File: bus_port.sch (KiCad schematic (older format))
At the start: 3 parts

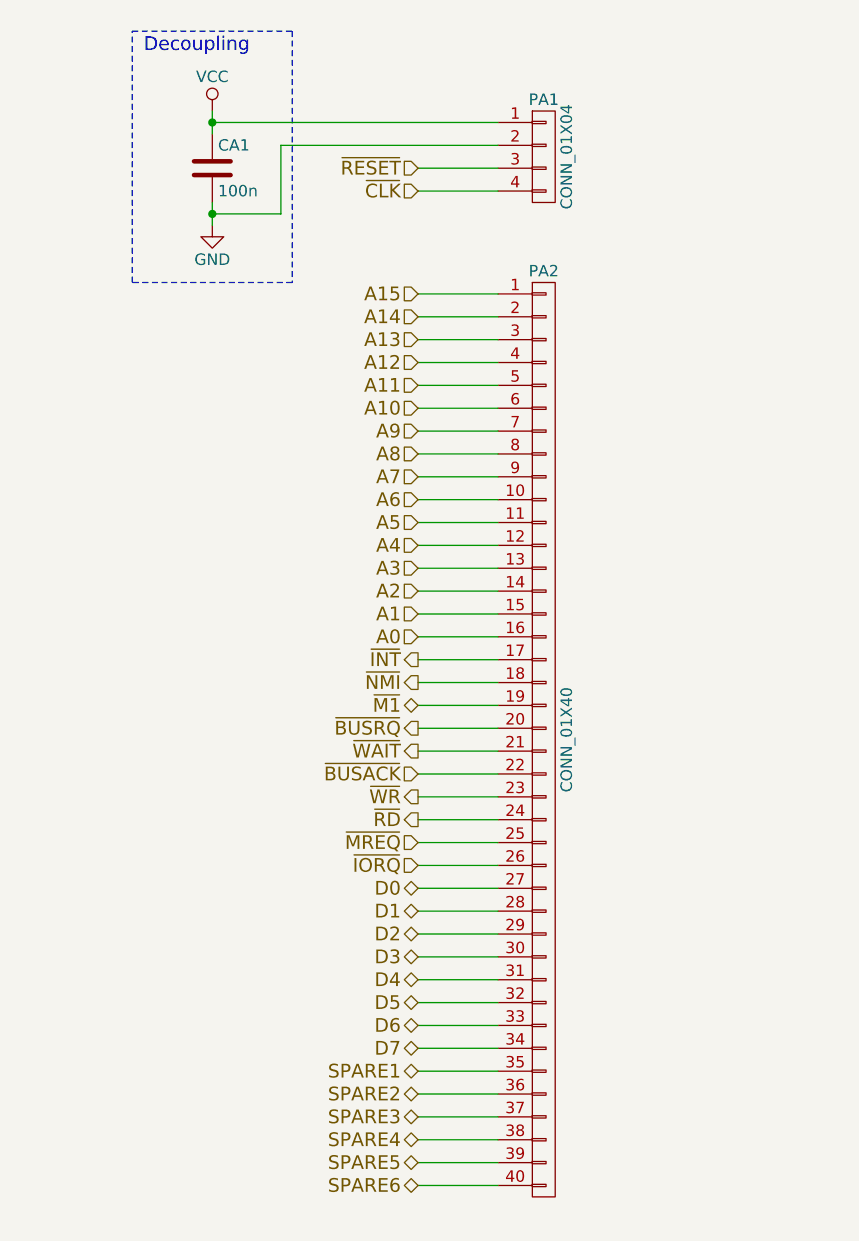
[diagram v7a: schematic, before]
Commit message: New layout complete. Now with rc2014 compat. slots!
Plus on board address decoding, single stepping using M1 line so button
is click per instruction. Board is also much smaller!
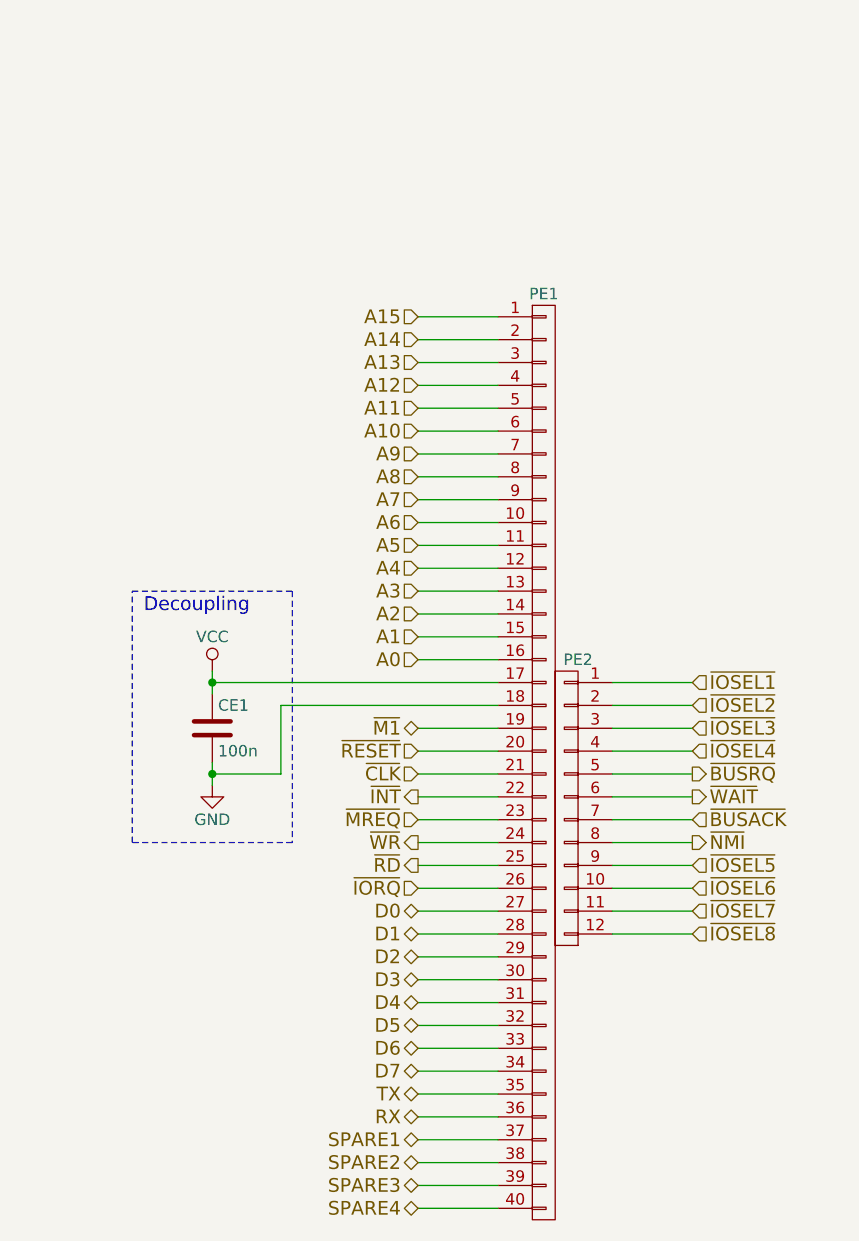
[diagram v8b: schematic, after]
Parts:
- removed PA1: CONN_01X04, Socket_Strips:Socket_Strip_Straight_1x04, symbol CONN_01X04
- removed PA2: CONN_01X40, Socket_Strips:Socket_Strip_Straight_1x40, symbol CONN_01X40
- added PA1: CONN_01X40, Socket_Strips:Socket_Strip_Straight_1x40, symbol CONN_01X40
- added PA2: CONN_01X12, Socket_Strips:Socket_Strip_Straight_1x12, symbol CONN_01X12
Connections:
- net A0: now also PA1.16 (P16)
- net A1: now also PA1.15 (P15)
- net A10: now also PA1.6 (P6)
- net A11: now also PA1.5 (P5)
- net A12: now also PA1.4 (P4)
- net A13: now also PA1.3 (P3)
- net A14: now also PA1.2 (P2)
- net A15: now also PA1.1 (P1)
- net A2: now also PA1.14 (P14)
- net A3: now also PA1.13 (P13)
- net A4: now also PA1.12 (P12)
- net A5: now also PA1.11 (P11)
- net A6: now also PA1.10 (P10)
- net A7: now also PA1.9 (P9)
- net A8: now also PA1.8 (P8)
- net A9: now also PA1.7 (P7)
- net D0: now also PA1.27 (P27)
- net D1: now also PA1.28 (P28)
- net D2: now also PA1.29 (P29)
- net D3: now also PA1.30 (P30)
- net D4: now also PA1.31 (P31)
- net D5: now also PA1.32 (P32)
- net D6: now also PA1.33 (P33)
- net D7: now also PA1.34 (P34)
- net GND: now also PA1.18 (P18)
- net SPARE1: now also PA1.37 (P37)
- net SPARE2: now also PA1.38 (P38)
- net SPARE3: now also PA1.39 (P39)
- net SPARE4: now also PA1.40 (P40)
- net VCC: now also PA1.17 (P17)
- net ~BUSACK: now also PA2.7 (P7)
- net ~BUSRQ: now also PA2.5 (P5)
- net ~CLK: now also PA1.21 (P21)
- net ~INT: now also PA1.22 (P22)
- net ~IORQ: now also PA1.26 (P26)
- net ~M1: now also PA1.19 (P19)
- net ~MREQ: now also PA1.23 (P23)
- net ~NMI: now also PA2.8 (P8)
- net ~RD: now also PA1.25 (P25)
- net ~RESET: now also PA1.20 (P20)
- net ~WAIT: now also PA2.6 (P6)
- net ~WR: now also PA1.24 (P24)
- new net RX: PA1.36 (P36)
- new net TX: PA1.35 (P35)
- new net ~IOSEL1: PA2.1 (P1)
- new net ~IOSEL2: PA2.2 (P2)
- new net ~IOSEL3: PA2.3 (P3)
- new net ~IOSEL4: PA2.4 (P4)
- new net ~IOSEL5: PA2.9 (P9)
- new net ~IOSEL6: PA2.10 (P10)
- new net ~IOSEL7: PA2.11 (P11)
- new net ~IOSEL8: PA2.12 (P12)
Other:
- moved on the sheet: CE1
